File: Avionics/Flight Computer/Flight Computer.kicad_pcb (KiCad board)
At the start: 4 copper layers, 50 x 40 mm, 202 parts, among them J1 AXK5S80047YG, J2 AXK5S80047YG, J3 473460001, J4 0734120110, J5 0734120110, J6 0734120110, U1 CC1310F128RGZR, U10 Logo, U11 Logo, U12 ATSAME70Q21A-AN, U13 NUF2042XV6, U2 CC1190RGVR, U3 CC2650F128RGZR, U4 CC2592RGVR, U5 MPU-9250, U6 LP5521YQ/NOPB, U7 LPS25HBTR, U8 TPS54232, U9 MAX-M8W-0, Y1 9HT11-32.768KDZB-T, Y2 7V-16.000MAHJ-T, Y3 XRCGB24M000F2P00R0, Y5 XRCGB24M000F2P00R0

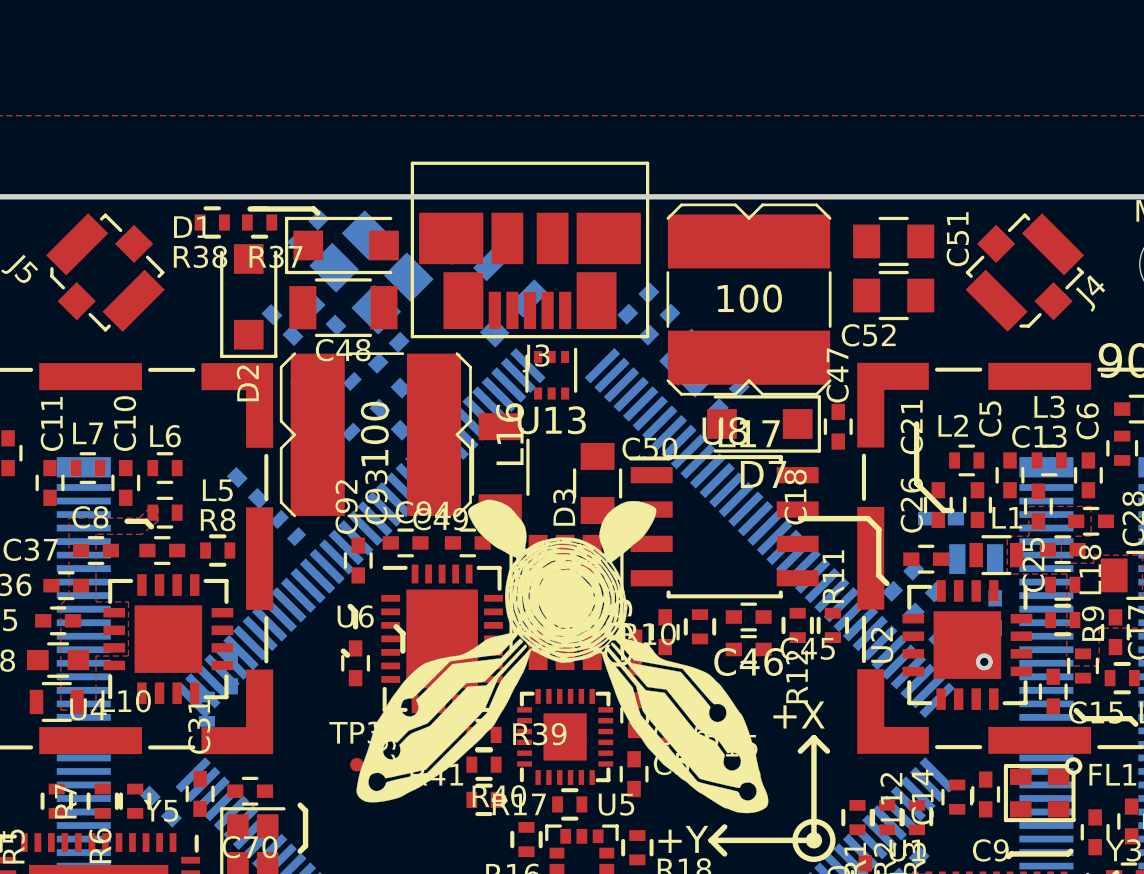
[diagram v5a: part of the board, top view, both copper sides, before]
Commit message: Reduced inductor size at small efficiency cost.
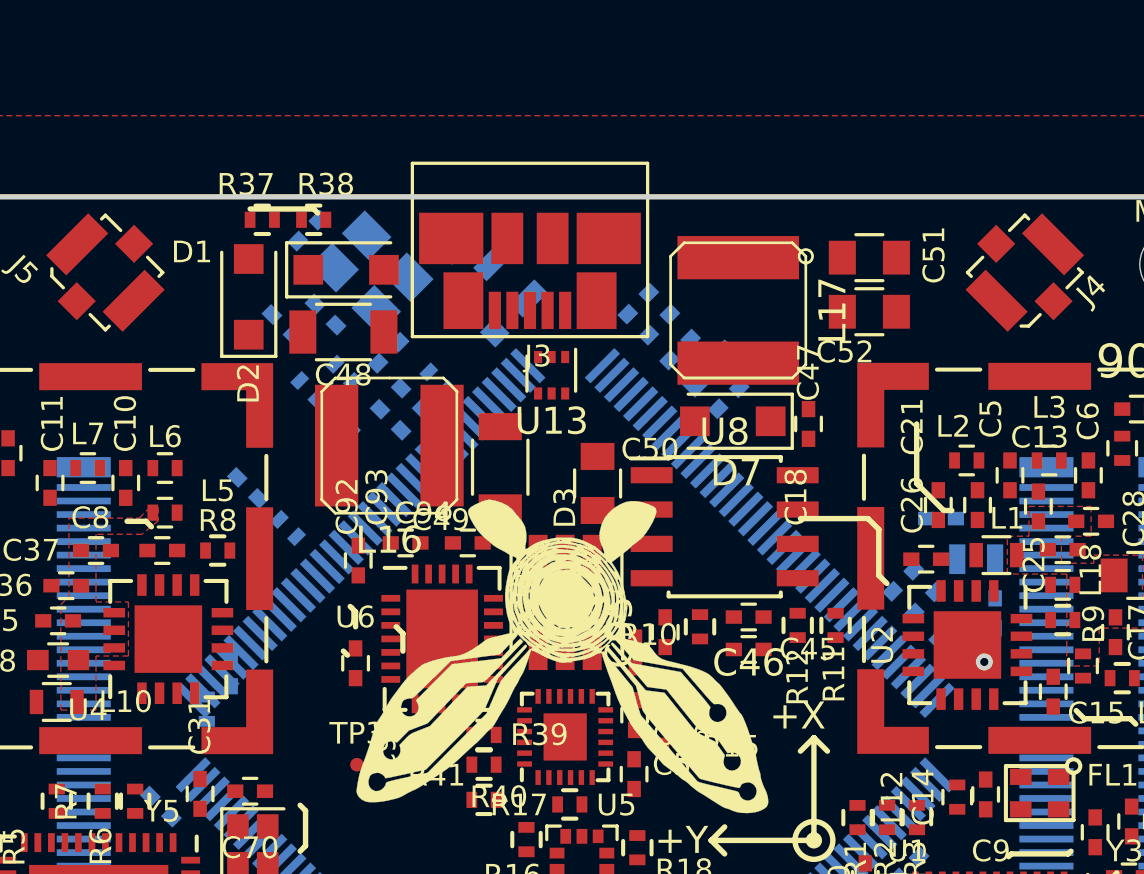
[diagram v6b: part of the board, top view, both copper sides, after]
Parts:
- L16, L17: value SRN6045-100M -> 74404052100; footprint Inductors_SMD:L_BOURNS-SRN6045 -> Inductors:Inductor_Wurth_LQS-5020
- moved R38 3.75 mm to (65.7, 85.9), turned to 180 degrees
- moved C47 1.10 mm to (84.0, 93.4)
- moved C52 1.08 mm to (86.2, 89.2)
- moved C51 1.08 mm to (86.2, 87.2)
- moved D7 1.00 mm to (81.2, 93.3)
- moved C48 0.90 mm to (66.8, 90.0)
- moved D1 0.90 mm to (66.9, 87.7)
- moved L16 0.64 mm to (68.5, 94.2)
- moved L17 0.57 mm to (81.4, 89.2), turned to 90 degrees
- moved R37 0.14 mm to (63.8, 85.9), turned to 180 degrees
- moved R11 0.10 mm to (85.0, 100.8), turned to 270 degrees
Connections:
- L17 pad 1: +3V3 -> Net-(C47-Pad1)
- L17 pad 2: Net-(C47-Pad1) -> +3V3

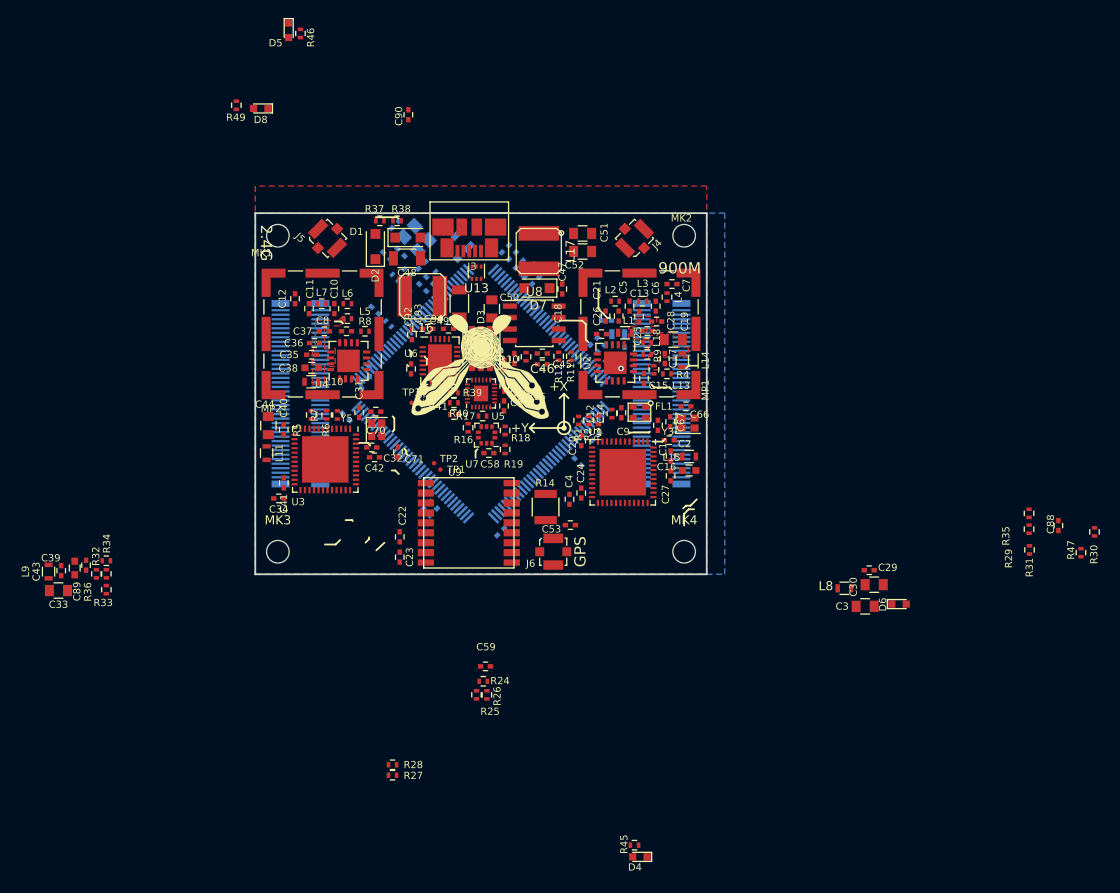
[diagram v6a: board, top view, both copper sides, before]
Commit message: Finished replacement and supply tuning
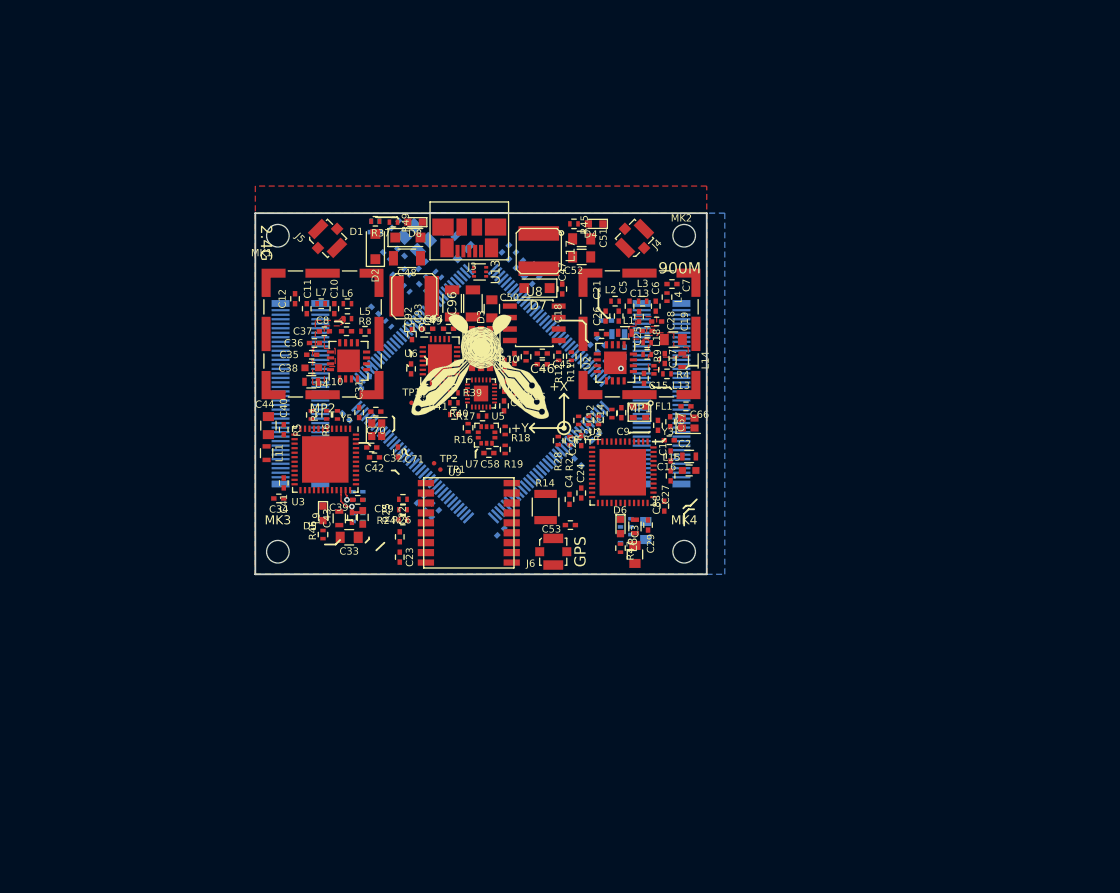
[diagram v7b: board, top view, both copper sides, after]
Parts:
- added C96: GRM31CR61H106MA12L, Capacitors_SMD:C_1206, F.Cu at (74.1, 95.0)
- C30, C59, C90, R29, R30, R31, R32, R33, R34, R35, R36, R38: moved to B.Cu
- MP1, MP2: value BMI-S-201-F -> BMI-S-101; footprint Shielding_Cabinets:Laird_Technologies_BMI-S-201-F_13.66x12.70mm -> Shielding_Cabinets:Laird_Technologies_BMI-S-101_13.66x12.70mm
- moved D4 70.3 mm to (87.7, 86.2)
- moved R45 69.1 mm to (85.3, 86.2), turned to 0 degrees
- moved R46 55.6 mm to (57.5, 120.6), turned to 90 degrees
- moved D5 53.6 mm to (57.5, 118.2)
- moved R30 51.4 mm to (91.6, 119.3), turned to 270 degrees
- moved R47 51.0 mm to (90.5, 122.1), turned to 90 degrees
- moved R35 45.3 mm to (90.5, 121.0), turned to 270 degrees
- moved R29 45.3 mm to (90.5, 119.3), turned to 270 degrees
- moved R31 44.2 mm to (91.6, 121.0)
- moved C88 43.7 mm to (95.3, 117.5)
- moved R27 41.9 mm to (84.8, 110.2), turned to 270 degrees
- moved R28 40.3 mm to (83.5, 110.2), turned to 270 degrees
- moved C33 32.7 mm to (60.4, 120.9)
- moved C43 32.7 mm to (60.7, 118.7)
- moved L9 32.7 mm to (59.3, 118.8)
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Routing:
- net /2.4 GHz Radio/VDDS_CC2650: track 0.00 -> 4.61 mm, vias 0 -> 1
- net /2.4 GHz Radio/~RESET: track 0.00 -> 1.79 mm, vias 0 -> 1

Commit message: Minor BOM fixes.
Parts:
- U13: value NUF2042XV6 -> NUF2042XV6T1G
- U8: value TPS54232 -> TPS54232DR
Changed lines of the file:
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@@
   (general
     (links 521)
-    (no_connects 312)
+    (no_connects 300)
     (area 49.900434 84.900075 100.100436 125.100077)
     (thickness 1.6)
@@
       (effects (font (size 1 1) (thickness 0.15)))
     )
-    (fp_text value NUF2042XV6 (at 0 1.75 270) (layer F.Fab)
+    (fp_text value NUF2042XV6T1G (at 0 1.75 270) (layer F.Fab)
       (effects (font (size 1 1) (thickness 0.15)))
     )
@@
       (effects (font (size 1 1) (thickness 0.15)))
     )
-    (fp_text value TPS54232 (at 0 3.5) (layer F.Fab)
-      (effects (font (size 1 1) (thickness 0.15)))
-    )
+    (fp_text value TPS54232DR (at 0 3.5) (layer F.Fab)
+      (effects (font (size 1 1) (thickness 0.15)))
+    )
